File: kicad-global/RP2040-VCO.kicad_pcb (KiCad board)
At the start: 2 copper layers, 80 x 128.5 mm, 57 parts, among them J1 Out, J2 Conn_01x06_Female, J3 Conn_01x06_Male, J4 Conn_01x08_Female, J5 Conn_01x08_Male, J6 V/oct, J7 Inv CV, J8 Power Input, SW1 SW_MEC_LOW_PROF_LED, SW2 SW_SPDT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

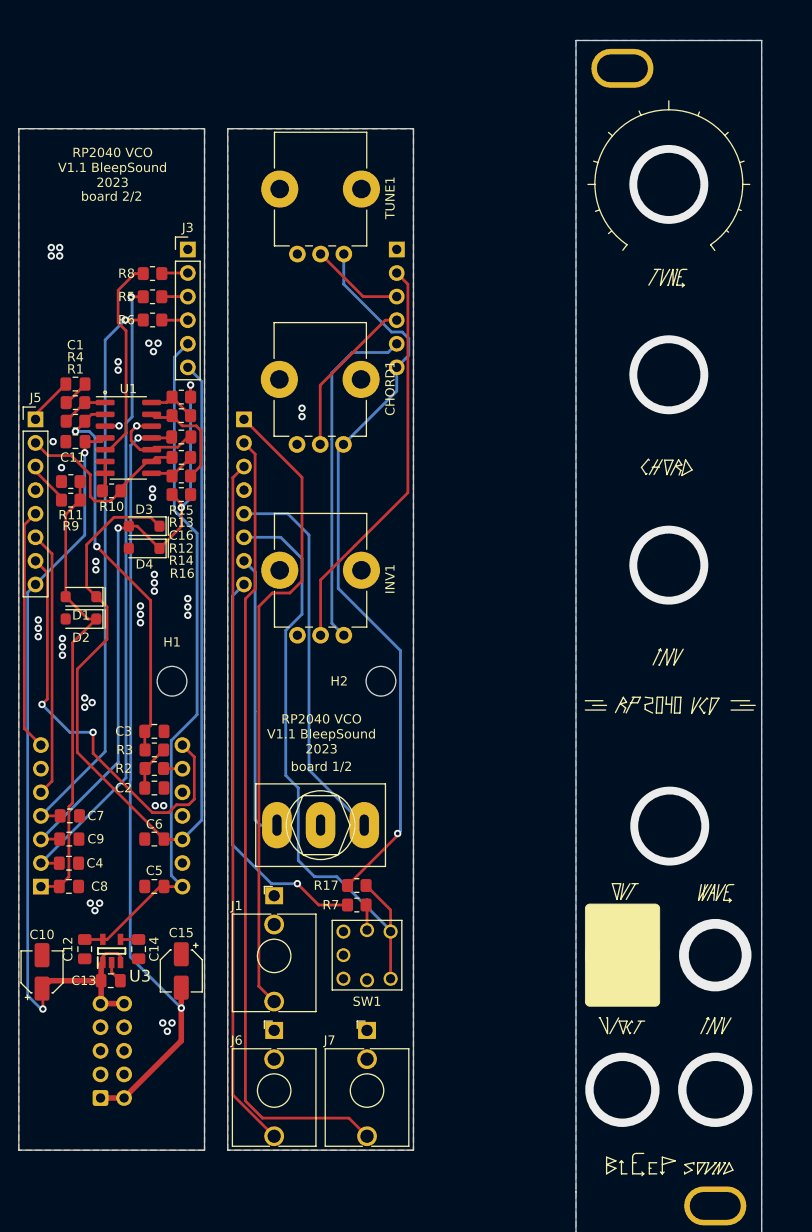
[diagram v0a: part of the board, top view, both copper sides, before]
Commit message: update pcb to v1.2 to fix switch issue with switch LED
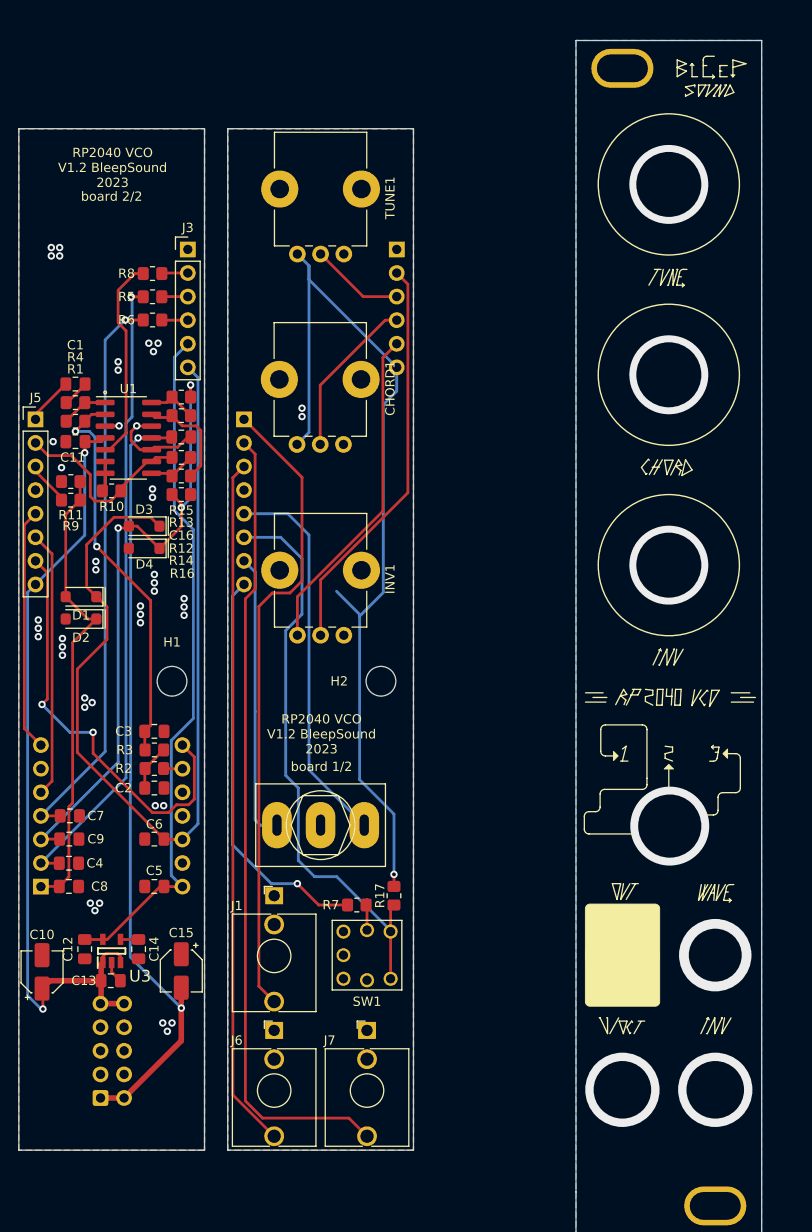
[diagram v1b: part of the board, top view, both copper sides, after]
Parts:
- moved R17 4.15 mm to (91.9, 119.1), turned to 90 degrees
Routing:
- net +3V3: track 181.5 -> 200.5 mm
- net /Push_SW: track 94.0 -> 90.9 mm
- net +5V: track 111.7 -> 110.1 mm
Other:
- board text added: "RP2040 VCO V1.2 BleepSound 2023"
- board text removed: "RP2040 VCO V1.1 BleepSound 2023"

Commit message: fix led button footprint
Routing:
- net Net-(R7-Pad1): track 3.30 -> 9.14 mm
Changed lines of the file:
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@@
         (effects (font (size 1 1) (thickness 0.15)))
     )
+    (fp_text user "+" (at -1.9 -2.6 unlocked) (layer "F.SilkS")
+        (effects (font (size 1 1) (thickness 0.15)) (justify left bottom))
+    )
     (fp_text user "${REFERENCE}" (at 0 10.16 unlocked) (layer "F.Fab")
         (effects (font (size 1 1) (thickness 0.15)))
@@
     (pad "4" thru_hole circle (at 2.54 -2.54) (size 1.524 1.524) (drill 1) (layers "*.Cu" "*.Mask")
       (net 18 "/Push_SW") (pinfunction "4") (pintype "passive"))
-    (pad "L1" thru_hole circle (at 0 -2.7) (size 1.524 1.524) (drill 1) (layers "*.Cu" "*.Mask")
+    (pad "L1" thru_hole circle (at 0 2.7) (size 1.524 1.524) (drill 1) (layers "*.Cu" "*.Mask")
       (net 34 "Net-(R7-Pad1)") (pinfunction "L1") (pintype "passive"))
-    (pad "L2" thru_hole circle (at 0 2.7) (size 1.524 1.524) (drill 1) (layers "*.Cu" "*.Mask")
+    (pad "L2" thru_hole circle (at 0 -2.7) (size 1.524 1.524) (drill 1) (layers "*.Cu" "*.Mask")
       (net 1 "GND") (pinfunction "L2") (pintype "passive"))
   )
@@
   (segment (start 70 64.1) (end 70 76.3) (width 0.3) (layer "B.Cu") (net 10))
   (segment (start 53.88 113.04) (end 62.2 104.72) (width 0.3) (layer "B.Cu") (net 10))
-  (segment (start 82 85.2) (end 82 74.05) (width 0.3) (layer "F.Cu") (net 11))
-  (segment (start 79 130.5) (end 77.35048 128.85048) (width 0.3) (layer "F.Cu") (net 11))
-  (segment (start 77.35048 128.85048) (end 77.35048 87.94952) (width 0.3) (layer "F.Cu") (net 11))
+  (segment (start 79.9 87.3) (end 82.1 85.1) (width 0.3) (layer "F.Cu") (net 11))
+  (segment (start 77.2 128.7) (end 77.2 88.1) (width 0.3) (layer "F.Cu") (net 11))
   (segment (start 53.3 67.2625) (end 56.5625 64) (width 0.3) (layer "F.Cu") (net 11))
-  (segment (start 82 74.05) (end 75.75 67.8) (width 0.3) (layer "F.Cu") (net 11))
-  (segment (start 78.8 86.5) (end 80.7 86.5) (width 0.3) (layer "F.Cu") (net 11))
-  (segment (start 77.35048 87.94952) (end 78.8 86.5) (width 0.3) (layer "F.Cu") (net 11))
-  (segment (start 80.7 86.5) (end 82 85.2) (width 0.3) (layer "F.Cu") (net 11))
+  (segment (start 79 130.5) (end 77.2 128.7) (width 0.3) (layer "F.Cu") (net 11))
+  (segment (start 82.1 74.15) (end 75.75 67.8) (width 0.3) (layer "F.Cu") (net 11))
+  (segment (start 82.1 85.1) (end 82.1 74.15) (width 0.3) (layer "F.Cu") (net 11))
+  (segment (start 78 87.3) (end 79.9 87.3) (width 0.3) (layer "F.Cu") (net 11))
   (segment (start 53.3 67.8) (end 53.3 67.2625) (width 0.3) (layer "F.Cu") (net 11))
+  (segment (start 77.2 88.1) (end 78 87.3) (width 0.3) (layer "F.Cu") (net 11))
   (segment (start 90.967919 57.12) (end 83.96 64.127919) (width 0.3) (layer "F.Cu") (net 12))
   (segment (start 92.2 57.12) (end 90.967919 57.12) (width 0.3) (layer "F.Cu") (net 12))
@@
   (segment (start 58.61 65.99) (end 58.6 66) (width 0.3) (layer "F.Cu") (net 33))
   (segment (start 58.6 66) (end 56.6 68) (width 0.3) (layer "F.Cu") (net 33))
-  (segment (start 89 119.5) (end 89 122.8) (width 0.3) (layer "F.Cu") (net 34))
+  (segment (start 90.2 127) (end 89 128.2) (width 0.3) (layer "F.Cu") (net 34))
+  (segment (start 88.9 120.1) (end 90.2 121.4) (width 0.3) (layer "F.Cu") (net 34))
+  (segment (start 90.2 121.4) (end 90.2 127) (width 0.3) (layer "F.Cu") (net 34))
   (segment (start 65.8 73.61) (end 67.71 73.61) (width 0.3) (layer "F.Cu") (net 35))
   (segment (start 70 71.9) (end 68 73.9) (width 0.3) (layer "F.Cu") (net 35))

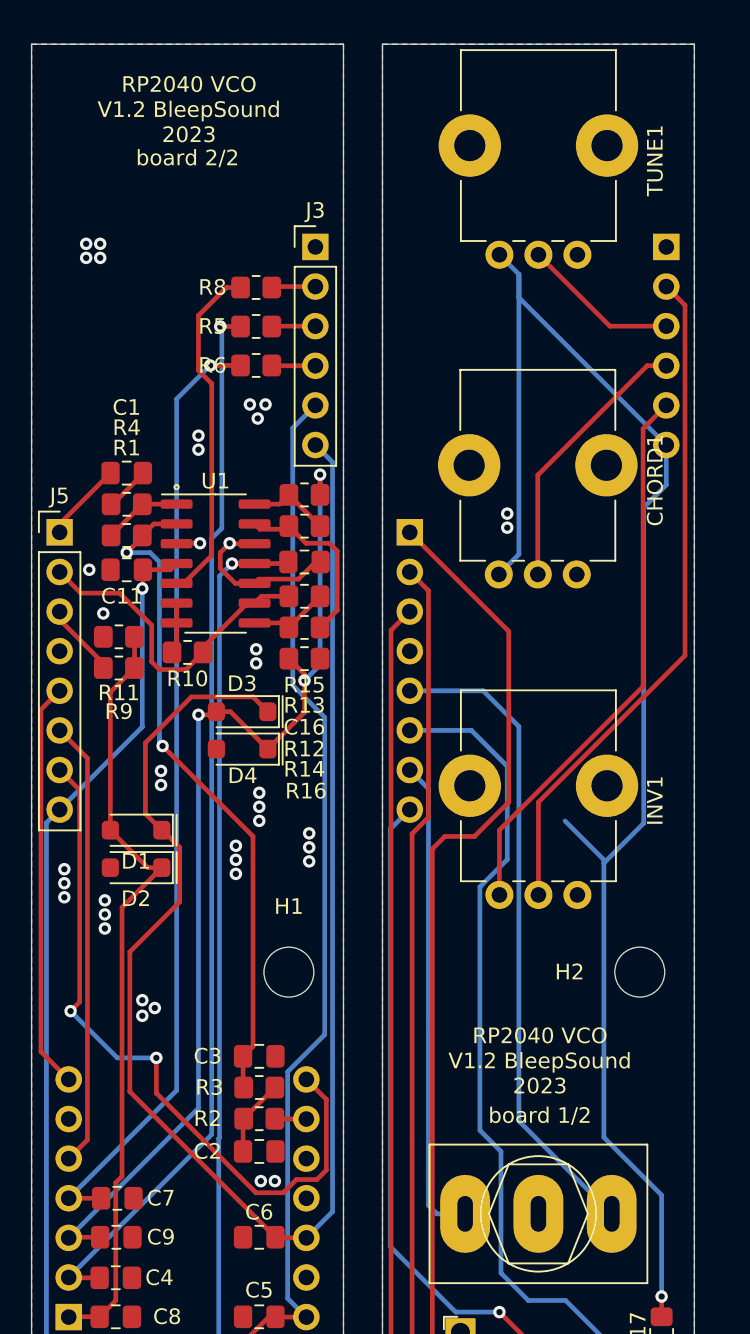
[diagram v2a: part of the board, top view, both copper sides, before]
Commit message: V1.4 update
add extra 10k resistor on inv CV input (missing)
Update BoM for clarity
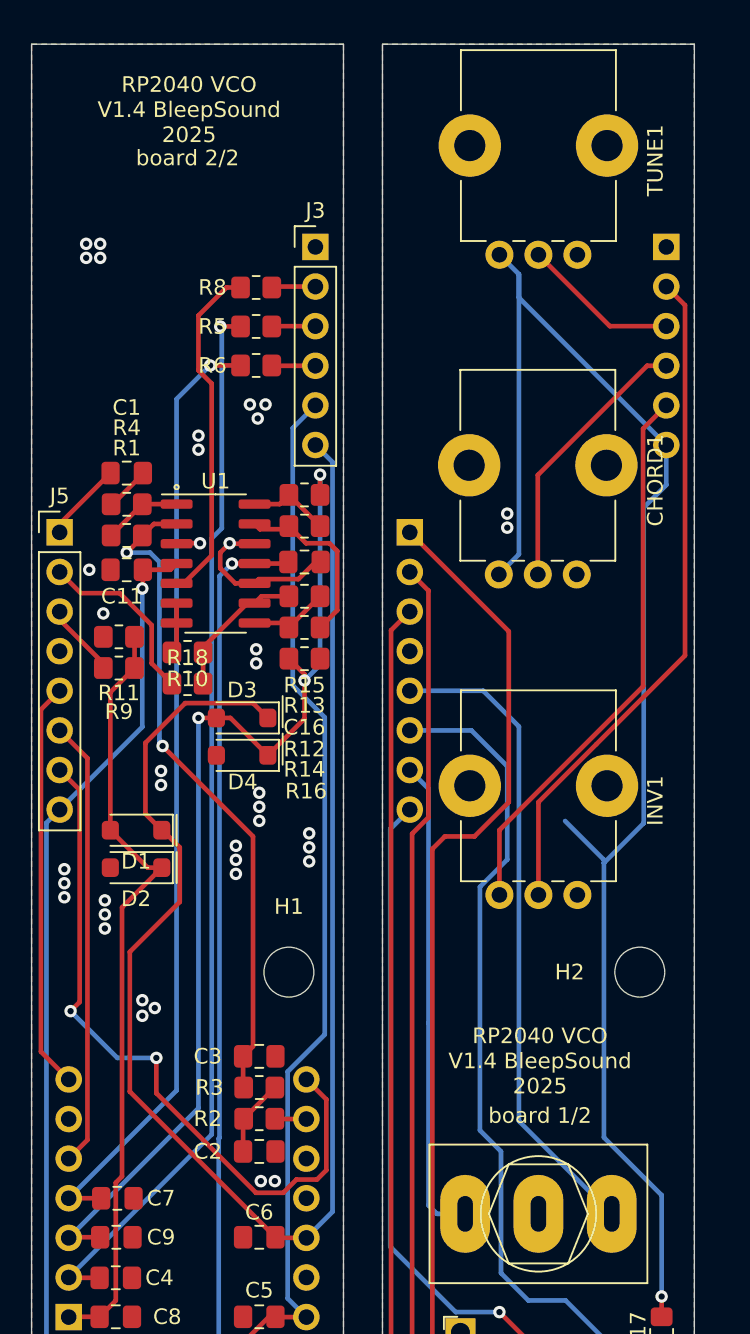
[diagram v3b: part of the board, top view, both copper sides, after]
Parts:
- added R18: 10k, Resistor_SMD:R_0805_2012Metric_Pad1.20x1.40mm_HandSolder, F.Cu at (61.5, 77.5)
- R7: value 2.2k -> 330R
- moved D3 0.40 mm to (65.0, 79.7)
- moved D4 0.40 mm to (65.0, 82.1)
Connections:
- R10 pad 2: /InvJack -> Net-(U1C--)
- R12 pad 1: /InvJack -> Net-(U1C--)
- U1 pad 9: /InvJack -> Net-(U1C--)
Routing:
- net /InvJack: track 107.3 -> 98.1 mm
- net Net-(U1C--): track 0.00 -> 9.18 mm
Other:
- board text added: "RP2040 VCO V1.4 BleepSound 2025"
- board text removed: "RP2040 VCO V1.2 BleepSound 2023"

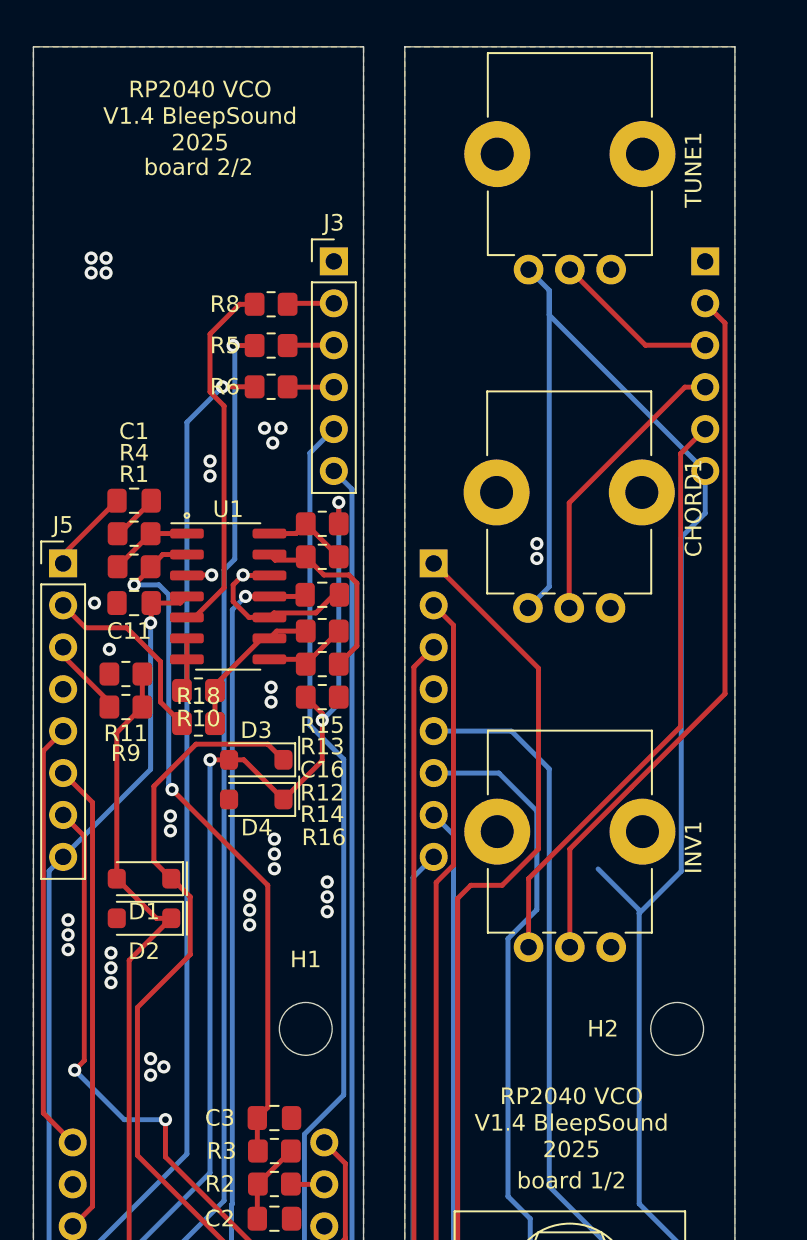
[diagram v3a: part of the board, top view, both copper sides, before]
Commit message: v1.5
reverse pots following issue raised on github
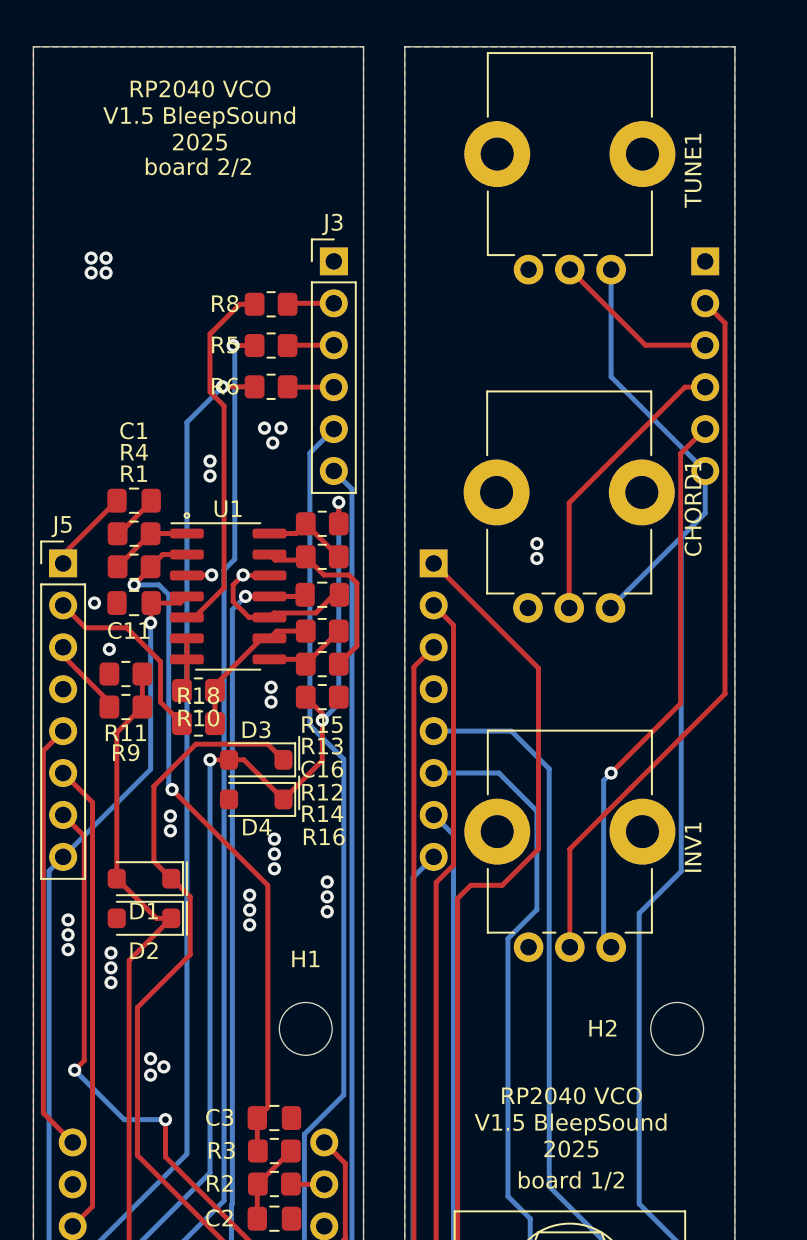
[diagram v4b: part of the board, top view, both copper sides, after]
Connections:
- CHORD1 pad 1: +3V3 -> GND
- CHORD1 pad 3: GND -> +3V3
- INV1 pad 1: +5V -> GND
- INV1 pad 3: GND -> +5V
- TUNE1 pad 1: +3V3 -> GND
- TUNE1 pad 3: GND -> +3V3
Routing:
- net +3V3: track 200.4 -> 180.8 mm
- net +5V: track 110.1 -> 108.4 mm, vias 0 -> 1
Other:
- board text added: "RP2040 VCO V1.5 BleepSound 2025"
- board text removed: "RP2040 VCO V1.4 BleepSound 2025"
